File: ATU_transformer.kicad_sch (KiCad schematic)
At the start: 137 parts, among them J1 Conn_Coaxial, K1 G2R-1-E DC12, K10 G2R-1-E DC12, K11 G2R-1-E DC12, K12 G2R-1-E DC12, K13 G2R-1-E DC12, K14 G2R-1-E DC12, K15 G2R-1-E DC12, K16 G2R-1-E DC12, K17 G2R-1-E DC12, K2 G2R-1-E DC12, K3 G2R-1-E DC12, K4 G2R-1-E DC12, K5 G2R-1-E DC12, K6 G2R-1-E DC12, K7 G2R-1-E DC12, K8 G2R-1-E DC12, K9 G2R-1-E DC12

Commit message: vswr and antenna switch schematic added
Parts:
- added C74, C75, C76, C77, C79, C81, C82, C83, C84: 10n, Capacitor_SMD:C_0805_2012Metric_Pad1.18x1.45mm_HandSolder, symbol Device:C_Small
- added C78: 10u, Capacitor_SMD:C_0805_2012Metric_Pad1.18x1.45mm_HandSolder, symbol Device:C_Small
- added C80: 100n, Capacitor_SMD:C_0805_2012Metric_Pad1.18x1.45mm_HandSolder, symbol Device:C_Small
- added D45, D46, D47, D48: 1N5711, symbol Device:D_Small
- added FB8, FB9: FerriteBead_Small, symbol Device:FerriteBead_Small
- added J7: Conn_Coaxial, symbol Connector:Conn_Coaxial
- added R23, R28: 100k, Resistor_SMD:R_0805_2012Metric_Pad1.20x1.40mm_HandSolder, symbol Device:R_Small
- added R24, R25, R26, R27, R37, R38: 100R, Resistor_SMD:R_1812_4532Metric_Pad1.30x3.40mm_HandSolder, symbol Device:R_Small
- added R29, R30: 1k, Resistor_SMD:R_0805_2012Metric_Pad1.20x1.40mm_HandSolder, symbol Device:R_Small
- added R31, R32: 22k, Resistor_SMD:R_0805_2012Metric_Pad1.20x1.40mm_HandSolder, symbol Device:R_Small
- added R33, R35: 15k, Resistor_SMD:R_0805_2012Metric_Pad1.20x1.40mm_HandSolder, symbol Device:R_Small
- added R34, R36: 18k, Resistor_SMD:R_0805_2012Metric_Pad1.20x1.40mm_HandSolder, symbol Device:R_Small
- added SW2: SW_SPDT, symbol Switch:SW_SPDT
- added T1, T2: CST1, Transformer_SMD:Transformer_Coilcraft_CST1, symbol Transformer:CST1
- added U1: LM358, symbol Amplifier_Operational:LM358
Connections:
- net +12V: now also C78.2, C79.2, C80.2, U1.8 (V+)
- net ATU_IN: now also SW2.2 (B), T1.7; no longer K1.3, K1.6, L1.1
- net GND: now also C74.2, C75.2, C76.2, C77.2, C78.1, C79.1, C80.1, C81.2, C82.2, C83.2, C84.2, J7.2 (Ext), R23.2, R24.1, R25.1, R26.2, R27.2, R28.2, R31.1, R32.1, R34.2, R36.2, R37.2, R38.2, T1.4, T2.6, U1.4 (V-)
- net +12V_R: now reaches C11.1, C17.1, C23.1, C29.1, C35.1, C4.1, C41.1, C47.1, C50.1, C54.1, D11.2 (A), D13.1 (K), D15.2 (A), D17.1 (K), D19.2 (A), D2.1 (K), D21.1 (K), D23.2 (A), D25.1 (K), D27.2 (A), D29.1 (K), D31.2 (A), D33.1 (K), D34.2 (A), D4.2 (A), D5.1 (K), D7.2 (A), D9.1 (K), FB1.2, K1.1, K11.1, K13.1, K15.1, K17.1, K3.1, K5.1, K7.1, K9.1
- new net: K1.3, K1.6, L1.1, SW2.1 (A)
- new net: C82.1, FB8.1, R33.2, R34.1
- new net: C75.1, C77.1, D46.1 (K), R28.1, R30.1
- new net: D46.2 (A), R24.2, R25.2, T1.6, T2.7
- new net: J7.1 (In), T1.8, T2.4
- new net: R33.1, U1.7
- new net: R37.1, R38.1, SW2.3 (C)
- new net: C83.1, FB9.1, R35.2, R36.1
- new net: D48.1 (K), R32.2, U1.6 (-)
- new net: C74.1, C76.1, D45.1 (K), R23.1, R29.1
- new net: D45.2 (A), R26.1, R27.1, T2.8
- new net: D47.1 (K), R31.2, U1.2 (-)
- new net: D47.2 (A), R35.1, U1.1
- new net: R30.2, U1.3 (+)
- new net: R29.2, U1.5 (+)
- new net FWD: C81.1, FB8.2
- new net REV: C84.1, FB9.2
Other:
- note added: "Aries Impedance transformer VSWR sensor"

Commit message: schematic fully captured
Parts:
- renumbered C49 to C1, C5 to C10, C1 to C11, C2 to C12, C78 to C13, C79 to C14, C4 to C15, C6 to C16, C80 to C17, C82 to C18, C83 to C19, C51 to C2, C81 to C20, C84 to C21, C7 to C22, C8 to C23, C9 to C24, C10 to C25, C11 to C26, C12 to C27, C13 to C28, C14 to C29, C74 to C3, C15 to C30, C16 to C31, C17 to C32, C18 to C33, C19 to C34, C20 to C35, C21 to C36, C22 to C37, C53 to C38, C23 to C39, C75 to C4, C24 to C40, C25 to C41, C26 to C42, C27 to C43, C54 to C44, C28 to C45, C29 to C46, C30 to C47, C31 to C48, C32 to C49, C50 to C5, C33 to C50, C34 to C51, C35 to C52, C36 to C53, C37 to C54, C38 to C55, C39 to C56, C40 to C57, C41 to C58, C42 to C59, C52 to C6, C43 to C60, C44 to C61, C45 to C62, C46 to C63, C47 to C64, C48 to C65, C76 to C7, C77 to C8, C3 to C9, D45 to D1, D6 to D10, D7 to D11, D8 to D12, D9 to D13, D10 to D14, D11 to D15, D12 to D16, D13 to D17, D14 to D18, D15 to D19, D46 to D2, D16 to D20, D33 to D21, D34 to D22, D17 to D23, D18 to D24, D19 to D25, D20 to D26, D21 to D27, D22 to D28, D23 to D29, D48 to D3, D24 to D30, D25 to D31, D26 to D32, D27 to D33, D28 to D34, D29 to D35, D30 to D36, D31 to D37, D32 to D38, D47 to D4, D2 to D5, D1 to D6, D4 to D7, D3 to D8, D5 to D9, FB8 to FB3, FB9 to FB4, H4 to H1, H3 to H2, H2 to H3, H1 to H4, J7 to J1, J1 to J2, K9 to K10, K10 to K11, K11 to K12, K12 to K13, K13 to K14, K14 to K15, K15 to K16, K16 to K17, K17 to K9, R26 to R1, R30 to R10, R32 to R11, R31 to R12, R2 to R13, R1 to R14, R33 to R15, R35 to R16, R34 to R17, R36 to R18, R3 to R19, R25 to R2, R4 to R20, R5 to R21, R6 to R22, R7 to R23, R8 to R24, R17 to R25, R9 to R26, R10 to R27, R11 to R28, R12 to R29, R27 to R3, R13 to R30, R14 to R31, R15 to R32, R16 to R33, R24 to R4, R23 to R5, R28 to R6, R37 to R7, R38 to R8, R29 to R9, SW2 to SW1
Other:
- note added: "Attention : Tous les connecteurs doivent être renumérotés pour rester cohérent avec les instructions de LA2NI et G8NJJ"

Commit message: component-footprint association
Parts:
- D1, D2, D3, D4: footprint (none) -> Diode_SMD:D_SOD-323_HandSoldering
- D10, D13, D14, D17, D18, D21, D23, D24, D27, D28, D31, D32, D35, D36, D5, D6, D9: value D_Small -> BAS16J; footprint (none) -> Diode_SMD:D_SOD-323_HandSoldering
- D11, D12, D16, D19, D20, D22, D25, D26, D29, D30, D33, D34, D37, D38, D7, D8: footprint (none) -> LED_SMD:LED_1206_3216Metric_Pad1.42x1.75mm_HandSolder
- D15: value LED_Small -> BAS16J; footprint (none) -> Diode_SMD:D_SOD-323_HandSoldering
- FB1, FB2: footprint (none) -> Inductor_SMD:L_2512_6332Metric_Pad1.52x3.35mm_HandSolder
- FB3, FB4: footprint (none) -> Inductor_SMD:L_0805_2012Metric_Pad1.15x1.40mm_HandSolder
- H1, H2, H3, H4: footprint (none) -> MountingHole:MountingHole_3.7mm_Pad
- L1, L2, L3, L4, L5, L6, L7, L8: footprint (none) -> Inductor_THT:L_Toroid_Horizontal_D25.4mm_P22.90mm_Vishay_TJ5_BigPads
- renumbered J1 to J14, J2 to J16
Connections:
- net at R15.1, U1.7: now also D3.2 (A)
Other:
- note added: "??"
- note added: "ATU IN"
- note added: "ATU OUT"
- note removed: "Attention : Tous les connecteurs doivent être renumérotés pour rester cohérent avec les instructions de LA2NI et G8NJJ"

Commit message: dual footprint for serial eprom
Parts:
- C11, C12: value C_Small -> 18p; footprint (none) -> Capacitor_Mica:Capacitor_Mica
- C24, C25: value C_Small -> 39p; footprint (none) -> Capacitor_Mica:Capacitor_Mica
- C30, C31: value C_Small -> 82p; footprint (none) -> Capacitor_Mica:Capacitor_Mica
- C36, C37: value C_Small -> 160p; footprint (none) -> Capacitor_Mica:Capacitor_Mica
- C43, C45: value C_Small -> 330p; footprint (none) -> Capacitor_Mica:Capacitor_Mica
- C50, C51: value C_Small -> 660p; footprint (none) -> Capacitor_Mica:Capacitor_Mica
- C56, C57: value C_Small -> 1320p; footprint (none) -> Capacitor_Mica:Capacitor_Mica
- C62, C63: value C_Small -> 2640p; footprint (none) -> Capacitor_Mica:Capacitor_Mica
- U1: footprint (none) -> Package_SO:SOIC-8_3.9x4.9mm_P1.27mm
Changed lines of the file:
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@@
       (effects (font (size 1.27 1.27)))
     )
-    (property "Value" "C_Small" (at 325.1263 118.634 90)
+    (property "Value" "1320p" (at 325.1263 118.634 90)
       (effects (font (size 1.27 1.27)))
     )
-    (property "Footprint" "" (at 325.12 121.285 0)
+    (property "Footprint" "Capacitor_Mica:Capacitor_Mica" (at 325.12 121.285 0)
       (effects (font (size 1.27 1.27)) hide)
     )
@@
       (effects (font (size 1.27 1.27)))
     )
-    (property "Value" "C_Small" (at 364.4963 118.634 90)
+    (property "Value" "2640p" (at 364.4963 118.634 90)
       (effects (font (size 1.27 1.27)))
     )
-    (property "Footprint" "" (at 364.49 121.285 0)
+    (property "Footprint" "Capacitor_Mica:Capacitor_Mica" (at 364.49 121.285 0)
       (effects (font (size 1.27 1.27)) hide)
     )
@@
       (effects (font (size 1.27 1.27)))
     )
-    (property "Value" "C_Small" (at 279.4063 118.634 90)
+    (property "Value" "660p" (at 279.4063 118.634 90)
       (effects (font (size 1.27 1.27)))
     )
-    (property "Footprint" "" (at 279.4 121.285 0)
+    (property "Footprint" "Capacitor_Mica:Capacitor_Mica" (at 279.4 121.285 0)
       (effects (font (size 1.27 1.27)) hide)
     )
@@
       (effects (font (size 1.27 1.27)))
     )
-    (property "Footprint" "" (at 88.265 215.9 0)
+    (property "Footprint" "Package_SO:SOIC-8_3.9x4.9mm_P1.27mm" (at 88.265 215.9 0)
       (effects (font (size 1.27 1.27)) hide)
     )
@@
       (effects (font (size 1.27 1.27)))
     )
-    (property "Value" "C_Small" (at 200.6663 118.634 90)
+    (property "Value" "160p" (at 200.6663 118.634 90)
       (effects (font (size 1.27 1.27)))
     )
-    (property "Footprint" "" (at 200.66 121.285 0)
+    (property "Footprint" "Capacitor_Mica:Capacitor_Mica" (at 200.66 121.285 0)
       (effects (font (size 1.27 1.27)) hide)
     )
@@
       (effects (font (size 1.27 1.27)))
     )
-    (property "Value" "C_Small" (at 82.5563 118.634 90)
+    (property "Value" "18p" (at 82.5563 118.634 90)
       (effects (font (size 1.27 1.27)))
     )
-    (property "Footprint" "" (at 82.55 121.285 0)
+    (property "Footprint" "Capacitor_Mica:Capacitor_Mica" (at 82.55 121.285 0)
       (effects (font (size 1.27 1.27)) hide)
     )
@@
       (effects (font (size 1.27 1.27)))
     )
-    (property "Value" "C_Small" (at 128.2763 118.634 90)
+    (property "Value" "39p" (at 128.2763 118.634 90)
       (effects (font (size 1.27 1.27)))
     )
-    (property "Footprint" "" (at 128.27 121.285 0)
+    (property "Footprint" "Capacitor_Mica:Capacitor_Mica" (at 128.27 121.285 0)
       (effects (font (size 1.27 1.27)) hide)
     )
@@
       (effects (font (size 1.27 1.27)))
     )
-    (property "Value" "C_Small" (at 240.0363 118.634 90)
+    (property "Value" "330p" (at 240.0363 118.634 90)
       (effects (font (size 1.27 1.27)))
     )
-    (property "Footprint" "" (at 240.03 121.285 0)
+    (property "Footprint" "Capacitor_Mica:Capacitor_Mica" (at 240.03 121.285 0)
       (effects (font (size 1.27 1.27)) hide)
     )
@@
       (effects (font (size 1.27 1.27)))
     )
-    (property "Value" "C_Small" (at 207.0163 118.634 90)
+    (property "Value" "160p" (at 207.0163 118.634 90)
       (effects (font (size 1.27 1.27)))
     )
-    (property "Footprint" "" (at 207.01 121.285 0)
+    (property "Footprint" "Capacitor_Mica:Capacitor_Mica" (at 207.01 121.285 0)
       (effects (font (size 1.27 1.27)) hide)
     )
@@
       (effects (font (size 1.27 1.27)))
     )
-    (property "Value" "C_Small" (at 318.7763 118.634 90)
+    (property "Value" "1320p" (at 318.7763 118.634 90)
       (effects (font (size 1.27 1.27)))
     )
-    (property "Footprint" "" (at 318.77 121.285 0)
+    (property "Footprint" "Capacitor_Mica:Capacitor_Mica" (at 318.77 121.285 0)
       (effects (font (size 1.27 1.27)) hide)
     )
@@
       (effects (font (size 1.27 1.27)))
     )
-    (property "Value" "C_Small" (at 161.2963 118.634 90)
+    (property "Value" "82p" (at 161.2963 118.634 90)
       (effects (font (size 1.27 1.27)))
     )
-    (property "Footprint" "" (at 161.29 121.285 0)
+    (property "Footprint" "Capacitor_Mica:Capacitor_Mica" (at 161.29 121.285 0)
       (effects (font (size 1.27 1.27)) hide)
     )
@@
       (effects (font (size 1.27 1.27)))
     )
-    (property "Value" "C_Small" (at 121.9263 118.634 90)
+    (property "Value" "39p" (at 121.9263 118.634 90)
       (effects (font (size 1.27 1.27)))
     )
-    (property "Footprint" "" (at 121.92 121.285 0)
+    (property "Footprint" "Capacitor_Mica:Capacitor_Mica" (at 121.92 121.285 0)
       (effects (font (size 1.27 1.27)) hide)
     )
@@
       (effects (font (size 1.27 1.27)))
     )
-    (property "Value" "C_Small" (at 285.7563 118.634 90)
+    (property "Value" "660p" (at 285.7563 118.634 90)
       (effects (font (size 1.27 1.27)))
     )
-    (property "Footprint" "" (at 285.75 121.285 0)
+    (property "Footprint" "Capacitor_Mica:Capacitor_Mica" (at 285.75 121.285 0)
       (effects (font (size 1.27 1.27)) hide)
     )
@@
       (effects (font (size 1.27 1.27)))
     )
-    (property "Footprint" "" (at 92.075 220.345 0)
+    (property "Footprint" "Package_SO:SOIC-8_3.9x4.9mm_P1.27mm" (at 92.075 220.345 0)
       (effects (font (size 1.27 1.27)) hide)
     )
@@
       (effects (font (size 1.27 1.27)))
     )
-    (property "Value" "C_Small" (at 358.1463 118.634 90)
+    (property "Value" "2640p" (at 358.1463 118.634 90)
       (effects (font (size 1.27 1.27)))
     )
-    (property "Footprint" "" (at 358.14 121.285 0)
+    (property "Footprint" "Capacitor_Mica:Capacitor_Mica" (at 358.14 121.285 0)
       (effects (font (size 1.27 1.27)) hide)
     )
@@
       (effects (font (size 1.27 1.27)))
     )
-    (property "Footprint" "" (at 92.075 205.105 0)
+    (property "Footprint" "Package_SO:SOIC-8_3.9x4.9mm_P1.27mm" (at 92.075 205.105 0)
       (effects (font (size 1.27 1.27)) hide)
     )
@@
       (effects (font (size 1.27 1.27)))
     )
-    (property "Value" "C_Small" (at 167.6463 118.634 90)
+    (property "Value" "82p" (at 167.6463 118.634 90)
       (effects (font (size 1.27 1.27)))
     )
-    (property "Footprint" "" (at 167.64 121.285 0)
+    (property "Footprint" "Capacitor_Mica:Capacitor_Mica" (at 167.64 121.285 0)
       (effects (font (size 1.27 1.27)) hide)
     )
@@
       (effects (font (size 1.27 1.27)))
     )
-    (property "Value" "C_Small" (at 246.3863 118.634 90)
+    (property "Value" "330p" (at 246.3863 118.634 90)
       (effects (font (size 1.27 1.27)))
     )
-    (property "Footprint" "" (at 246.38 121.285 0)
+    (property "Footprint" "Capacitor_Mica:Capacitor_Mica" (at 246.38 121.285 0)
       (effects (font (size 1.27 1.27)) hide)
     )
@@
       (effects (font (size 1.27 1.27)))
     )
-    (property "Value" "C_Small" (at 88.9063 118.634 90)
+    (property "Value" "18p" (at 88.9063 118.634 90)
       (effects (font (size 1.27 1.27)))
     )
-    (property "Footprint" "" (at 88.9 121.285 0)
+    (property "Footprint" "Capacitor_Mica:Capacitor_Mica" (at 88.9 121.285 0)
       (effects (font (size 1.27 1.27)) hide)
     )

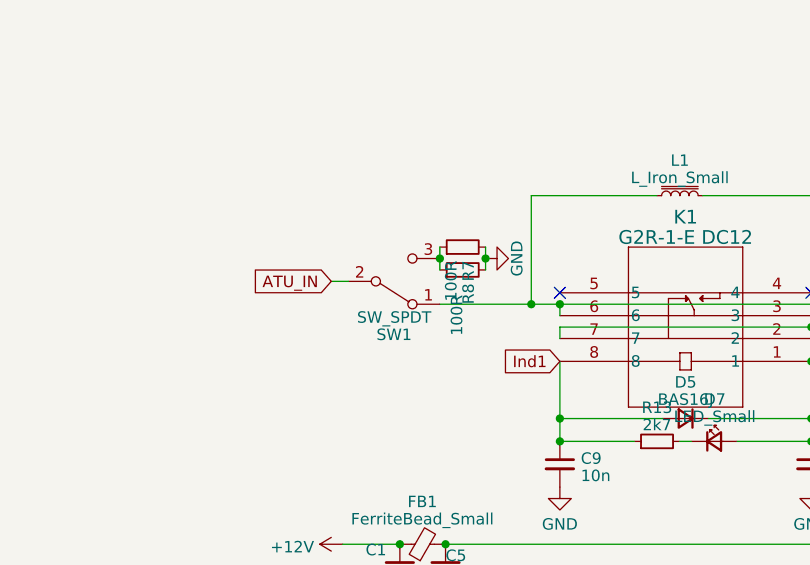
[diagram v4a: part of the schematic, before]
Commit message: all component sourced, all 3D object configured
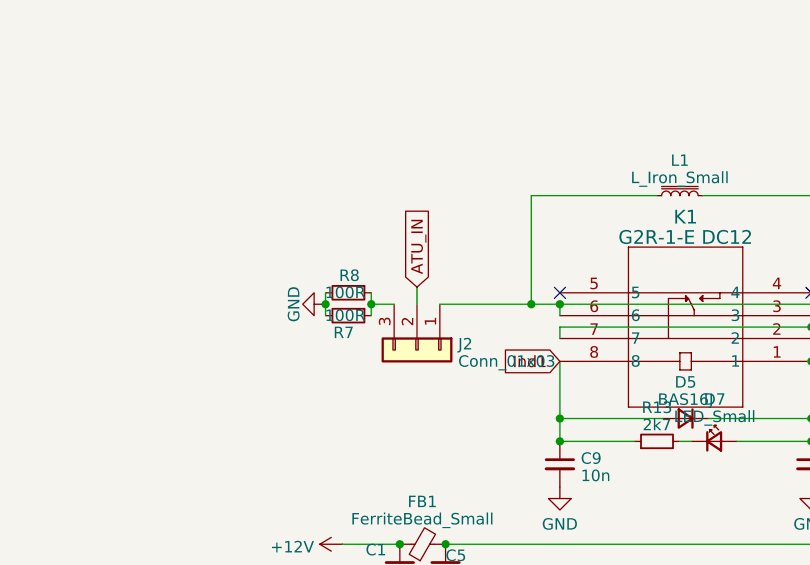
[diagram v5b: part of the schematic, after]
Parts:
- removed SW1: SW_SPDT, symbol Switch:SW_SPDT
- added J2: Conn_01x03, Connector_Molex:Molex_KK-396_A-41791-0003_1x03_P3.96mm_Vertical, symbol Connector_Generic:Conn_01x03
- J14, J16: footprint (none) -> BNC_Amphenol_031-5329-51RFX:BNC_Amphenol_031532951RFX
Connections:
- net ATU_IN: now also J2.2 (Pin_2)
- net at K1.3, K1.6, L1.1: now also J2.1 (Pin_1)
- net at R7.1, R8.1: now also J2.3 (Pin_3)
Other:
- moved on the sheet: R7, R8
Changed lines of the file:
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@@
   (junction (at 276.86 145.415) (diameter 0) (color 0 0 0 0)
   )
-  (junction (at 71.755 39.37) (diameter 0) (color 0 0 0 0)
+  (junction (at 53.975 44.45) (diameter 0) (color 0 0 0 0)
   )
   (junction (at 344.17 149.225) (diameter 0) (color 0 0 0 0)
@@
   (junction (at 384.81 32.385) (diameter 0) (color 0 0 0 0)
   )
+  (junction (at 59.055 44.45) (diameter 0) (color 0 0 0 0)
+  )
   (junction (at 42.545 205.105) (diameter 0) (color 0 0 0 0)
   )
@@
   (junction (at 99.695 220.345) (diameter 0) (color 0 0 0 0)
   )
-  (junction (at 66.675 39.37) (diameter 0) (color 0 0 0 0)
-  )
   (junction (at 383.54 149.225) (diameter 0) (color 0 0 0 0)
   )
@@
     (stroke (width 0) (type default))
   )
-  (wire (pts (xy 71.755 39.37) (xy 71.755 40.64))
+  (wire (pts (xy 53.975 44.45) (xy 53.975 43.18))
     (stroke (width 0) (type default))
   )
@@
     (stroke (width 0) (type default))
   )
-  (wire (pts (xy 54.61 41.91) (xy 56.515 41.91))
+  (wire (pts (xy 64.135 42.545) (xy 64.135 44.45))
     (stroke (width 0) (type default))
   )
@@
     (stroke (width 0) (type default))
   )
-  (wire (pts (xy 66.675 38.1) (xy 66.675 39.37))
+  (wire (pts (xy 59.055 45.72) (xy 59.055 44.45))
     (stroke (width 0) (type default))
   )
@@
     (stroke (width 0) (type default))
   )
-  (wire (pts (xy 71.755 38.1) (xy 71.755 39.37))
+  (wire (pts (xy 53.975 45.72) (xy 53.975 44.45))
     (stroke (width 0) (type default))
   )
@@
     (stroke (width 0) (type default))
   )
+  (wire (pts (xy 59.055 44.45) (xy 61.595 44.45))
+    (stroke (width 0) (type default))
+  )
   (wire (pts (xy 187.96 32.385) (xy 174.625 32.385))
     (stroke (width 0) (type default))
@@
     (stroke (width 0) (type default))
   )
+  (wire (pts (xy 59.055 44.45) (xy 59.055 43.18))
+    (stroke (width 0) (type default))
+  )
   (wire (pts (xy 119.38 133.35) (xy 119.38 133.985))
     (stroke (width 0) (type default))
@@
     (stroke (width 0) (type default))
   )
-  (wire (pts (xy 66.675 39.37) (xy 66.675 40.64))
-    (stroke (width 0) (type default))
-  )
   (wire (pts (xy 360.68 121.285) (xy 361.95 121.285))
     (stroke (width 0) (type default))
@@
     )
   )
-  (global_label "ATU_IN" (shape input) (at 54.61 41.91 180) (fields_autoplaced)
-    (effects (font (size 1.27 1.27)) (justify right))
-    (property "Intersheetrefs" "${INTERSHEET_REFS}" (at 45.4146 41.91 0)
-      (effects (font (size 1.27 1.27)) (justify right) hide)
+  (global_label "ATU_IN" (shape input) (at 64.135 42.545 90) (fields_autoplaced)
+    (effects (font (size 1.27 1.27)) (justify left))
+    (property "Intersheetrefs" "${INTERSHEET_REFS}" (at 64.135 33.3496 90)
+      (effects (font (size 1.27 1.27)) (justify left) hide)
     )
   )
@@
     )
   )
-  (symbol (lib_id "Device:R_Small") (at 69.215 40.64 90) (unit 1)
+  (symbol (lib_id "Device:R_Small") (at 56.515 43.18 270) (unit 1)
     (in_bom yes) (on_board yes) (dnp no)
-    (property "Reference" "R8" (at 69.8587 42.1386 0)
+    (property "Reference" "R8" (at 57.785 41.275 90)
       (effects (font (size 1.27 1.27)) (justify right))
     )
-    (property "Value" "100R" (at 68.5727 43.4086 0)
+    (property "Value" "100R" (at 58.42 43.18 90)
       (effects (font (size 1.27 1.27)) (justify right))
     )
-    (property "Footprint" "Resistor_SMD:R_1812_4532Metric_Pad1.30x3.40mm_HandSolder" (at 69.215 40.64 0)
+    (property "Footprint" "Resistor_SMD:R_1812_4532Metric_Pad1.30x3.40mm_HandSolder" (at 56.515 43.18 0)
       (effects (font (size 1.27 1.27)) hide)
     )
-    (property "Datasheet" "~" (at 69.215 40.64 0)
+    (property "Datasheet" "~" (at 56.515 43.18 0)
       (effects (font (size 1.27 1.27)) hide)
     )
@@
     )
   )
+  (symbol (lib_id "Connector_Generic:Conn_01x03") (at 64.135 49.53 270) (unit 1)
+    (in_bom yes) (on_board yes) (dnp no) (fields_autoplaced)
+    (property "Reference" "J2" (at 68.707 48.8863 90)
+      (effects (font (size 1.27 1.27)) (justify left))
+    )
+    (property "Value" "Conn_01x03" (at 68.707 50.8073 90)
+      (effects (font (size 1.27 1.27)) (justify left))
+    )
+    (property "Footprint" "Connector_Molex:Molex_KK-396_A-41791-0003_1x03_P3.96mm_Vertical" (at 64.135 49.53 0)
+      (effects (font (size 1.27 1.27)) hide)
+    )
+    (property "Datasheet" "~" (at 64.135 49.53 0)
+      (effects (font (size 1.27 1.27)) hide)
+    )
+    (pin "1")
+    (pin "2")
+    (pin "3")
+    (instances
+      (project "K_Aries"
+        (path "/4d56c8f7-829b-457e-80cb-74e9f55628bb/d6e8d14c-e765-45cf-852c-f558c754ac0c"
+          (reference "J2") (unit 1)
+        )
+      )
+    )
+  )
   (symbol (lib_id "Device:C_Small") (at 200.66 121.285 90) (unit 1)
     (in_bom yes) (on_board yes) (dnp no) (fields_autoplaced)
@@
       (effects (font (size 1.27 1.27)) (justify left))
     )
-    (property "Footprint" "" (at 399.415 32.385 0)
+    (property "Footprint" "BNC_Amphenol_031-5329-51RFX:BNC_Amphenol_031532951RFX" (at 399.415 32.385 0)
       (effects (font (size 1.27 1.27)) hide)
     )
@@
     )
   )
-  (symbol (lib_id "Device:R_Small") (at 69.215 38.1 90) (unit 1)
-    (in_bom yes) (on_board yes) (dnp no) (fields_autoplaced)
-    (property "Reference" "R7" (at 69.8587 39.5986 0)
+  (symbol (lib_id "Device:R_Small") (at 56.515 45.72 270) (unit 1)
+    (in_bom yes) (on_board yes) (dnp no)
+    (property "Reference" "R7" (at 57.15 47.625 90)
       (effects (font (size 1.27 1.27)) (justify right))
     )
-    (property "Value" "100R" (at 67.9377 39.5986 0)
+    (property "Value" "100R" (at 58.42 45.72 90)
       (effects (font (size 1.27 1.27)) (justify right))
     )
-    (property "Footprint" "Resistor_SMD:R_1812_4532Metric_Pad1.30x3.40mm_HandSolder" (at 69.215 38.1 0)
+    (property "Footprint" "Resistor_SMD:R_1812_4532Metric_Pad1.30x3.40mm_HandSolder" (at 56.515 45.72 0)
       (effects (font (size 1.27 1.27)) hide)
     )
-    (property "Datasheet" "~" (at 69.215 38.1 0)
+    (property "Datasheet" "~" (at 56.515 45.72 0)
       (effects (font (size 1.27 1.27)) hide)
     )
@@
     )
   )
-  (symbol (lib_id "power:GND") (at 71.755 39.37 90) (unit 1)
+  (symbol (lib_id "power:GND") (at 53.975 44.45 270) (unit 1)
     (in_bom yes) (on_board yes) (dnp no) (fields_autoplaced)
-    (property "Reference" "#PWR012" (at 78.105 39.37 0)
+    (property "Reference" "#PWR012" (at 47.625 44.45 0)
       (effects (font (size 1.27 1.27)) hide)
     )
-    (property "Value" "GND" (at 75.2569 39.37 0)
+    (property "Value" "GND" (at 50.4731 44.45 0)
       (effects (font (size 1.27 1.27)))
     )
-    (property "Footprint" "" (at 71.755 39.37 0)
+    (property "Footprint" "" (at 53.975 44.45 0)
       (effects (font (size 1.27 1.27)) hide)
     )
-    (property "Datasheet" "" (at 71.755 39.37 0)
+    (property "Datasheet" "" (at 53.975 44.45 0)
       (effects (font (size 1.27 1.27)) hide)
     )
@@
     )
   )
-  (symbol (lib_id "Switch:SW_SPDT") (at 61.595 41.91 0) (mirror x) (unit 1)
-    (in_bom yes) (on_board yes) (dnp no)
-    (property "Reference" "SW1" (at 61.595 47.8409 0)
-      (effects (font (size 1.27 1.27)))
-    )
-    (property "Value" "SW_SPDT" (at 61.595 45.9199 0)
-      (effects (font (size 1.27 1.27)))
-    )
-    (property "Footprint" "" (at 61.595 41.91 0)
-      (effects (font (size 1.27 1.27)) hide)
-    )
-    (property "Datasheet" "~" (at 61.595 41.91 0)
-      (effects (font (size 1.27 1.27)) hide)
-    )
-    (pin "1")
-    (pin "2")
-    (pin "3")
-    (instances
-      (project "K_Aries"
-        (path "/4d56c8f7-829b-457e-80cb-74e9f55628bb/d6e8d14c-e765-45cf-852c-f558c754ac0c"
-          (reference "SW1") (unit 1)
-        )
-      )
-    )
-  )
   (symbol (lib_id "Device:C_Small") (at 128.27 121.285 90) (unit 1)
     (in_bom yes) (on_board yes) (dnp no) (fields_autoplaced)
@@
       (effects (font (size 1.27 1.27)))
     )
-    (property "Footprint" "" (at 26.67 224.79 0)
+    (property "Footprint" "BNC_Amphenol_031-5329-51RFX:BNC_Amphenol_031532951RFX" (at 26.67 224.79 0)
       (effects (font (size 1.27 1.27)) hide)
     )
